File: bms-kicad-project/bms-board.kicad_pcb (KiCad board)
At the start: 4 copper layers, 134 parts, among them J1 12402012E212A, J2 DEBUG, J3 Conn_02x18_Odd_Even, J4 Conn_02x18_Odd_Even, Q1 BSS308PE_H6327, Q10 BSS308PE_H6327, Q11 BSS308PE_H6327, Q12 BSS308PE_H6327, Q13 BSS308PE_H6327, Q2 BSS308PE_H6327, Q3 BSS308PE_H6327, Q4 BSS308PE_H6327, Q5 BSS308PE_H6327, Q6 BSS308PE_H6327, Q7 BSS308PE_H6327, Q8 BSS308PE_H6327, Q9 BSS308PE_H6327, SW1 KMR223G LFG, SW2 KMR223G LFG, U1 LTC6804-2, U2 W25Q128JVSIQ TR, U3 NCP1117ST33T3G, U4 RP2040, X1 ABM8-272-T3

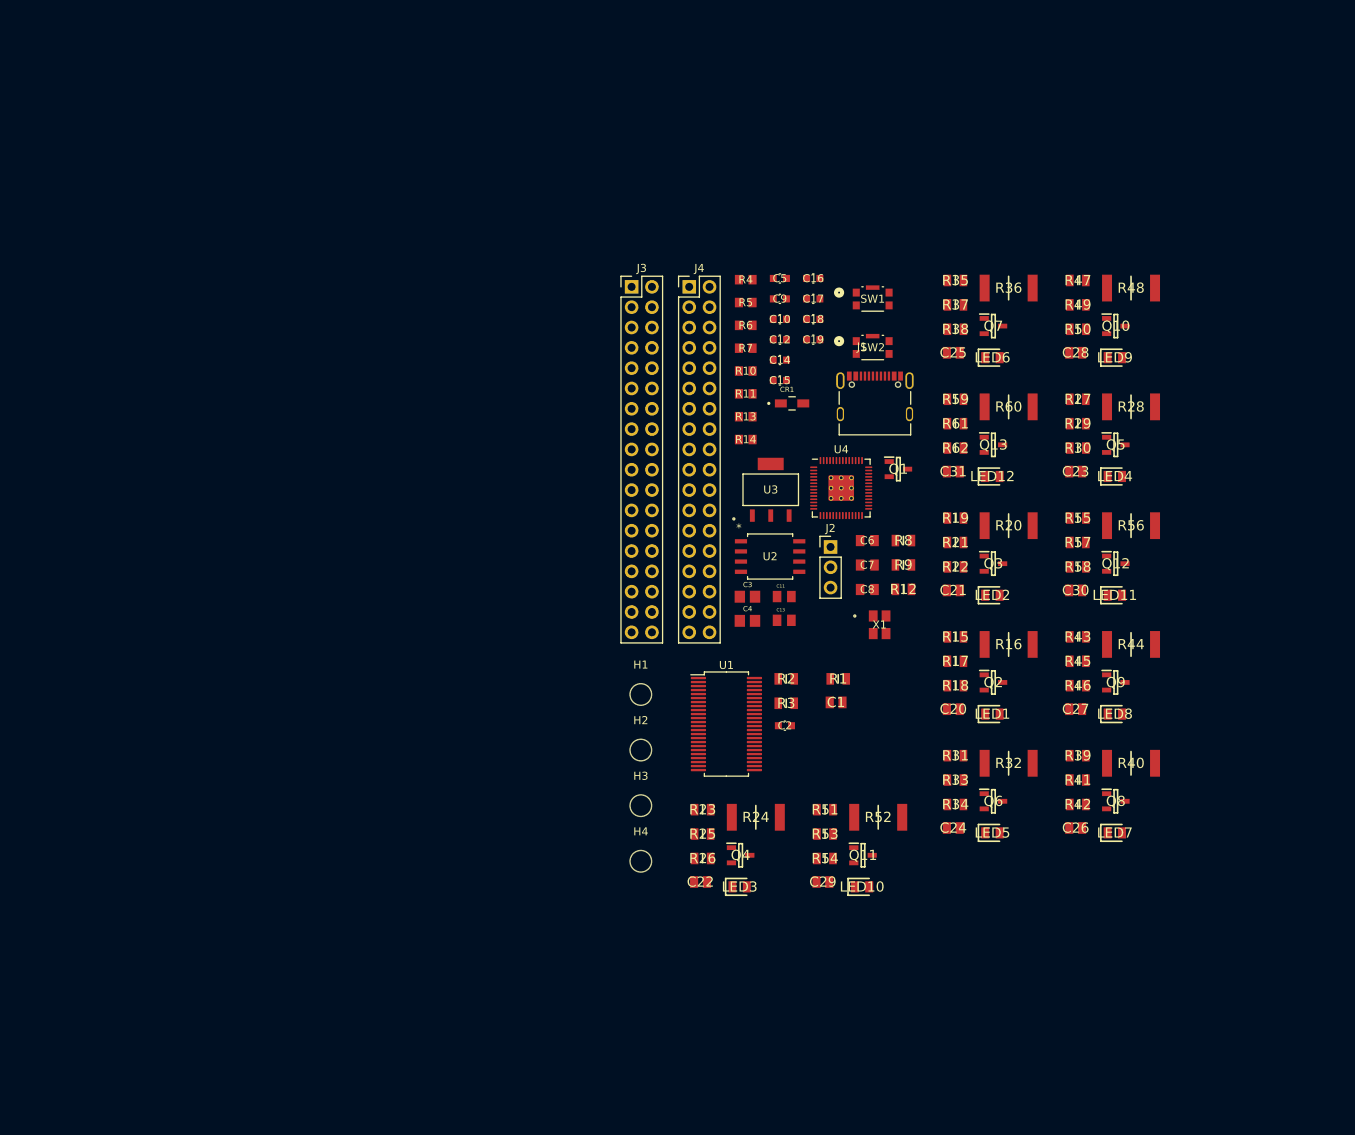
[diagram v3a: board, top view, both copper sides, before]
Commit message: feat: Added 0OHM jumper between ULTRASONIC and VDD, added LED indicator for PGOOD
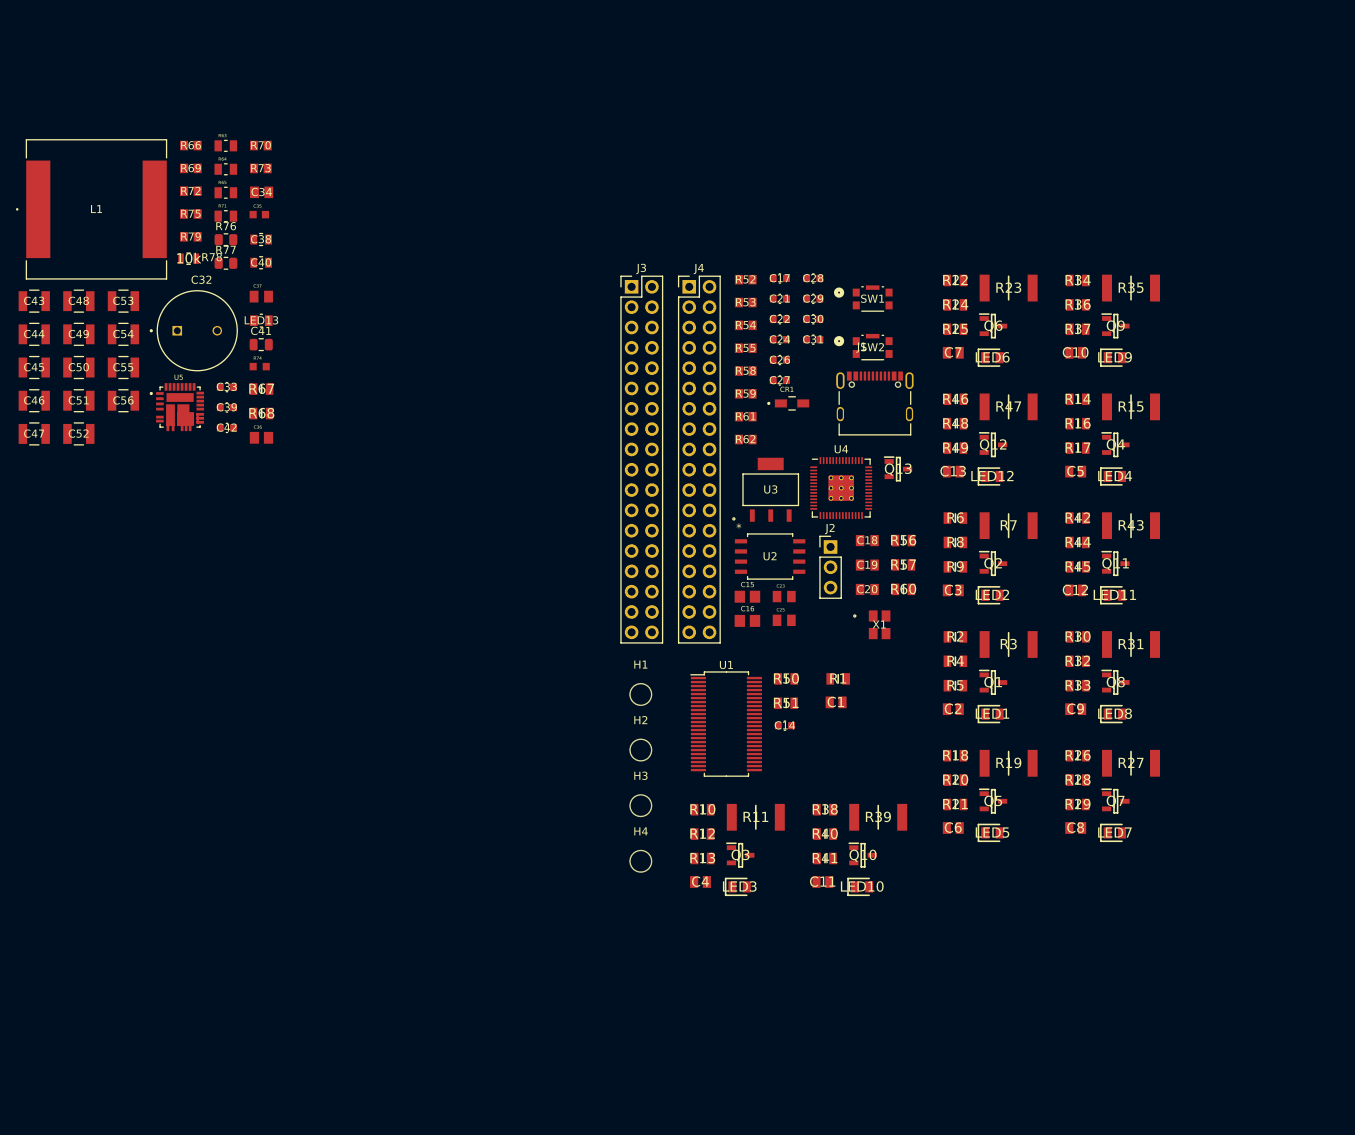
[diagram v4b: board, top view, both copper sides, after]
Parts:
- added C32: 220u, FixedWing:CAPPRD500W60D1000H2500, F.Cu at (52.3, 68.4)
- added C33: 0.1µ, FixedWing:CAP_GCJ-18_MUR, F.Cu at (56.0, 75.4)
- added C34: 560p, FixedWing:CAP_CC0805_YAG, F.Cu at (60.3, 51.1)
- added C35: 1u, FixedWing:CAPC1608X90N, F.Cu at (60.0, 53.9)
- added C36: 33n, FixedWing:CAPC2012X94N, F.Cu at (60.3, 81.8)
- added C37: 4.7u, FixedWing:CAPC2012X145N, F.Cu at (60.3, 64.1)
- added C38: 3.9n, FixedWing:G-21_MUR, F.Cu at (60.3, 57.0)
- added C39: 0.1µ, FixedWing:CAP_GCJ-18_MUR, F.Cu at (56.0, 78.0)
- added C40: 1.5n, FixedWing:G-21_MUR, F.Cu at (60.3, 59.9)
- added C41: C, Capacitor_SMD:C_0805_2012Metric, F.Cu at (60.3, 70.1)
- added C42: 0.1µ, FixedWing:CAP_GCJ-18_MUR, F.Cu at (56.0, 80.5)
- added C43: 47u, FixedWing:G-32_MUR, F.Cu at (31.9, 64.7)
- added C44: 47u, FixedWing:G-32_MUR, F.Cu at (31.9, 68.8)
- added C45: 47u, FixedWing:G-32_MUR, F.Cu at (31.9, 73.0)
- added C46: 47u, FixedWing:G-32_MUR, F.Cu at (31.9, 77.1)
- added C47: 47u, FixedWing:G-32_MUR, F.Cu at (31.9, 81.3)
- added C48: 47u, FixedWing:G-32_MUR, F.Cu at (37.5, 64.7)
- added C49: 47u, FixedWing:G-32_MUR, F.Cu at (37.5, 68.8)
- added C50: 47u, FixedWing:G-32_MUR, F.Cu at (37.5, 73.0)
- added C51: 47u, FixedWing:G-32_MUR, F.Cu at (37.5, 77.1)
- added C52: 47u, FixedWing:G-32_MUR, F.Cu at (37.5, 81.3)
- added C53: 47u, FixedWing:G-32_MUR, F.Cu at (43.0, 64.7)
- added C54: 47u, FixedWing:G-32_MUR, F.Cu at (43.0, 68.8)
- added C55: 47u, FixedWing:G-32_MUR, F.Cu at (43.0, 73.0)
- added C56: 47u, FixedWing:G-32_MUR, F.Cu at (43.0, 77.1)
- added L1: 5.6u, FixedWing:IND_IHLP-6767GZ_VIS, F.Cu at (39.7, 53.2)
- added LED13: LTST-C170KGKT, FixedWing:LED_LTST-C170KGKT_LTO, F.Cu at (60.3, 67.1)
- added R63: 562k, FixedWing:RESC2012X60N, F.Cu at (55.8, 45.3)
- added R64: 100k, FixedWing:RESC2012X60N, F.Cu at (55.8, 48.2)
- added R65: 100k, FixedWing:RESC2012X60N, F.Cu at (55.8, 51.1)
- added R66: 523k, FixedWing:RC0805N_YAG, F.Cu at (51.5, 45.2)
- added R67: 100, FixedWing:RESC2012X50N, F.Cu at (60.3, 75.7)
- added R68: 475, FixedWing:RESC2012X50N, F.Cu at (60.3, 78.7)
- added R69: 1k, FixedWing:RC0805N_YAG, F.Cu at (51.5, 48.1)
- added R70: 41.2, FixedWing:RC0805N_VIS, F.Cu at (60.2, 45.2)
- added R71: 100k, FixedWing:RESC2012X60N, F.Cu at (55.8, 54.1)
- added R72: 1k, FixedWing:RC0805N_YAG, F.Cu at (51.5, 50.9)
- added R73: 93.1k, FixedWing:RC0805N_PAN, F.Cu at (60.2, 48.1)
- added R74: 3.3, FixedWing:RESC1608X55N, F.Cu at (60.1, 72.9)
- added R75: 11.5k, FixedWing:RC0805N_YAG, F.Cu at (51.5, 53.8)
- added R76: R, Resistor_SMD:R_0805_2012Metric, F.Cu at (55.9, 57.0)
- added R77: R, Resistor_SMD:R_0805_2012Metric, F.Cu at (55.9, 60.0)
- added R78: 10k, FixedWing:KOA_Speer-RK73H2A-0-0-MFG, F.Cu at (51.2, 59.4)
- added R79: 56.2k, FixedWing:RC0805N_YAG, F.Cu at (51.5, 56.7)
- added U5: SIC461ED-T1-GE3, FixedWing:CONV_SIC461ED-T1-GE3, F.Cu at (50.1, 77.9)
- R13: renamed from R26; value 3k3 -> 3.3k
- R17: renamed from R30; value 3k3 -> 3.3k
- R21: renamed from R34; value 3k3 -> 3.3k
- R25: renamed from R38; value 3k3 -> 3.3k
- R29: renamed from R42; value 3k3 -> 3.3k
- R33: renamed from R46; value 3k3 -> 3.3k
- R37: renamed from R50; value 3k3 -> 3.3k
- R41: renamed from R54; value 3k3 -> 3.3k
- R45: renamed from R58; value 3k3 -> 3.3k
- R49: renamed from R62; value 3k3 -> 3.3k
- R5: renamed from R18; value 3k3 -> 3.3k
- R50: renamed from R2; value 3k3 -> 3.3k
- R56: renamed from R8; value 3k3 -> 3.3k
- R57: renamed from R9; value 3k3 -> 3.3k
- R60: renamed from R12; value 3k3 -> 3.3k
- R9: renamed from R22; value 3k3 -> 3.3k
- renumbered C28 to C10, C29 to C11, C30 to C12, C31 to C13, C2 to C14, C3 to C15, C4 to C16, C5 to C17, C6 to C18, C7 to C19, C20 to C2, C8 to C20, C9 to C21, C10 to C22, C11 to C23, C12 to C24, C13 to C25, C14 to C26, C15 to C27, C16 to C28, C17 to C29, C21 to C3, C18 to C30, C19 to C31, C22 to C4, C23 to C5, C24 to C6, C25 to C7, C26 to C8, C27 to C9, Q2 to Q1, Q11 to Q10, Q12 to Q11, Q13 to Q12, Q1 to Q13, Q3 to Q2, Q4 to Q3, Q5 to Q4, Q6 to Q5, Q7 to Q6, Q8 to Q7, Q9 to Q8, Q10 to Q9, R23 to R10, R24 to R11, R25 to R12, R27 to R14, R28 to R15, R29 to R16, R31 to R18, R32 to R19, R15 to R2, R33 to R20, R35 to R22, R36 to R23, R37 to R24, R39 to R26, R40 to R27, R41 to R28, R16 to R3, R43 to R30, R44 to R31, R45 to R32, R47 to R34, R48 to R35, R49 to R36, R51 to R38, R52 to R39, R17 to R4, R53 to R40, R55 to R42, R56 to R43, R57 to R44, R59 to R46, R60 to R47, R61 to R48, R3 to R51, R4 to R52, R5 to R53, R6 to R54, R7 to R55, R10 to R58, R11 to R59, R19 to R6, R13 to R61, R14 to R62, R20 to R7, R21 to R8
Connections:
- C1 pad 2: GND -> +5V
- C14 pad 2: GND -> +5V
- C15 pad 1: GND -> +5V
- C16 pad 1: GND -> +5V
- C17 pad 1: GND -> +5V
- C18 pad 1: GND -> +5V
- C19 pad 2: GND -> +5V
- C20 pad 1: GND -> +5V
- C21 pad 1: GND -> +5V
- C22 pad 1: GND -> +5V
- C23 pad 1: GND -> +5V
- C24 pad 1: GND -> +5V
- C25 pad 1: GND -> +5V
- C26 pad 1: GND -> +5V
- C27 pad 1: GND -> +5V
- C28 pad 1: GND -> +5V
- C29 pad 1: GND -> +5V
- C30 pad 1: GND -> +5V
- C31 pad 1: GND -> +5V
- J1 pad A1_B12: GND -> +5V
- J1 pad B1_A12: GND -> +5V
- J1 pad SH1: GND -> +5V
- J1 pad SH2: GND -> +5V
- J1 pad SH3: GND -> +5V
- J1 pad SH4: GND -> +5V
- J2 pad 2: GND -> +5V
- J3 pad 1: GND -> +5V
- J3 pad 11: GND -> +5V
- J3 pad 13: GND -> +5V
- J3 pad 15: GND -> +5V
- J3 pad 17: GND -> +5V
- J3 pad 19: GND -> +5V
- J3 pad 21: GND -> +5V
- J3 pad 23: GND -> +5V
- J3 pad 25: GND -> +5V
- J3 pad 27: GND -> +5V
- J3 pad 29: GND -> +5V
- J3 pad 3: GND -> +5V
- J3 pad 31: GND -> +5V
- J3 pad 33: GND -> +5V
- J3 pad 35: GND -> +5V
- J3 pad 36: GND -> +5V
- J3 pad 5: GND -> +5V
- J3 pad 7: GND -> +5V
- J3 pad 9: GND -> +5V
- J4 pad 10: GND -> +5V
- J4 pad 12: GND -> +5V
- J4 pad 14: GND -> +5V
- J4 pad 16: GND -> +5V
- J4 pad 18: GND -> +5V
- J4 pad 2: GND -> +5V
- J4 pad 20: GND -> +5V
- J4 pad 22: GND -> +5V
- J4 pad 24: GND -> +5V
- J4 pad 26: GND -> +5V
- J4 pad 28: GND -> +5V
- J4 pad 30: GND -> +5V
- J4 pad 32: GND -> +5V
- J4 pad 34: GND -> +5V
- J4 pad 35: GND -> +5V
- J4 pad 36: GND -> +5V
- J4 pad 4: GND -> +5V
- J4 pad 6: GND -> +5V
- J4 pad 8: GND -> +5V
- R2 pad 1: GND -> +5V
- R3 pad 1: GND -> +5V
- R4 pad 1: GND -> +5V
- R52 pad 2: GND -> +5V
- R53 pad 2: GND -> +5V
- SW1 pad 3: GND -> +5V
- SW1 pad 4: GND -> +5V
- SW1 pad 5: GND -> +5V
- SW2 pad 3: GND -> +5V
- SW2 pad 4: GND -> +5V
- SW2 pad 5: GND -> +5V
- U1 pad 30: GND -> +5V
- U1 pad 31: GND -> +5V
- U1 pad 40: GND -> +5V
- U3 pad 1: GND -> +5V
- U4 pad 19: GND -> +5V
- U4 pad 57: GND -> +5V
- X1 pad 2: GND -> +5V
- X1 pad 4: GND -> +5V

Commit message: feat: added buncha shit, refer to tasks 4 and 8
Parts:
- added H5: MountingHole_Pad, MountingHole:MountingHole_3.2mm_M3_Pad_Via, F.Cu at (148.0, 88.7)
- added H6: MountingHole_Pad, MountingHole:MountingHole_3.2mm_M3_Pad_Via, F.Cu at (148.0, 96.7)
- added H7: MountingHole_Pad, MountingHole:MountingHole_3.2mm_M3_Pad_Via, F.Cu at (156.0, 88.7)
- added H8: MountingHole_Pad, MountingHole:MountingHole_3.2mm_M3_Pad_Via, F.Cu at (156.0, 96.7)
- added L10: 600Ω, FixedWing:IND_BLM31PG391SN1L_MUR, F.Cu at (159.1, 75.5)
- added L11: 600Ω, FixedWing:IND_BLM31PG391SN1L_MUR, F.Cu at (164.9, 61.7)
- added L12: 600Ω, FixedWing:IND_BLM31PG391SN1L_MUR, F.Cu at (164.9, 65.1)
- added L13: 600Ω, FixedWing:IND_BLM31PG391SN1L_MUR, F.Cu at (164.9, 68.6)
- added L14: 600Ω, FixedWing:IND_BLM31PG391SN1L_MUR, F.Cu at (164.9, 72.1)
- added L15: 600Ω, FixedWing:IND_BLM31PG391SN1L_MUR, F.Cu at (175.3, 86.5)
- added L16: 5.6u, FixedWing:IND_IHLP-6767GZ_VIS, F.Cu at (99.3, 119.2)
- added L2: 600Ω, FixedWing:IND_BLM31PG391SN1L_MUR, F.Cu at (153.3, 65.1)
- added L3: 600Ω, FixedWing:IND_BLM31PG391SN1L_MUR, F.Cu at (153.3, 68.6)
- added L4: 600Ω, FixedWing:IND_BLM31PG391SN1L_MUR, F.Cu at (153.3, 72.1)
- added L5: 600Ω, FixedWing:IND_BLM31PG391SN1L_MUR, F.Cu at (153.3, 75.5)
- added L6: 600Ω, FixedWing:IND_BLM31PG391SN1L_MUR, F.Cu at (159.1, 61.7)
- added L7: 600Ω, FixedWing:IND_BLM31PG391SN1L_MUR, F.Cu at (159.1, 65.1)
- added L8: 600Ω, FixedWing:IND_BLM31PG391SN1L_MUR, F.Cu at (159.1, 68.6)
- added L9: 600Ω, FixedWing:IND_BLM31PG391SN1L_MUR, F.Cu at (159.1, 72.1)
- added R80: 1k, FixedWing:RC0805N_YAG, F.Cu at (114.8, 96.0)
- added R81: 5.6k, FixedWing:RESC2012X60N, F.Cu at (116.6, 82.6)
- added R82: 27, FixedWing:RC0805N_YAG, F.Cu at (114.8, 98.9)
- added R83: 27, FixedWing:RC0805N_YAG, F.Cu at (114.8, 101.7)
- added R84: 562k, FixedWing:RESC2012X60N, F.Cu at (115.5, 111.2)
- added R85: 100k, FixedWing:RESC2012X60N, F.Cu at (115.5, 114.1)
- added R86: 100k, FixedWing:RESC2012X60N, F.Cu at (115.5, 117.1)
- added R87: 1k, FixedWing:RC0805N_YAG, F.Cu at (111.1, 111.2)
- added R88: 5.6k, FixedWing:RESC2012X60N, F.Cu at (115.5, 120.0)
- added R89: 1k, FixedWing:RC0805N_YAG, F.Cu at (111.1, 114.0)
- added R90: 41.2, FixedWing:RC0805N_VIS, F.Cu at (119.8, 122.9)
- added R91: 93.1k, FixedWing:RC0805N_PAN, F.Cu at (119.8, 125.8)
- added R92: 523k, FixedWing:RC0805N_YAG, F.Cu at (111.1, 116.9)
- added R93: 0, FixedWing:RC1206N_YAG, F.Cu at (120.4, 111.4)
- added R94: 3.3, FixedWing:RESC1608X55N, F.Cu at (119.7, 135.8)
- added R95: 10k, FixedWing:KOA_Speer-RK73H2A-0-0-MFG, F.Cu at (110.8, 125.3)
- added R96: 11.5k, FixedWing:RC0805N_YAG, F.Cu at (111.1, 119.7)
- added R97: R, Resistor_SMD:R_0805_2012Metric, F.Cu at (119.9, 141.6)
- added R98: R, Resistor_SMD:R_0805_2012Metric, F.Cu at (119.9, 144.5)
- added R99: 56.2k, FixedWing:RC0805N_YAG, F.Cu at (111.1, 122.6)
- C34: value 560p -> 33n; footprint FixedWing:CAP_CC0805_YAG -> FixedWing:CAPC2012X94N
- C36: value 33n -> 560p; footprint FixedWing:CAPC2012X94N -> FixedWing:CAP_CC0805_YAG
- H1, H2, H3, H4: value MountingHole -> MountingHole_Pad; footprint MountingHole:MountingHole_2.7mm_M2.5 -> MountingHole:MountingHole_3.2mm_M3_Pad_Via
- L1: value 5.6u -> 600Ω; footprint FixedWing:IND_IHLP-6767GZ_VIS -> FixedWing:IND_BLM31PG391SN1L_MUR
- LED13: value LTST-C170KGKT -> LTST-C170KRKT; footprint FixedWing:LED_LTST-C170KGKT_LTO -> FixedWing:LEDC2012X120N
- R10, R14, R18, R2, R22, R26, R6: value 475 -> 0; footprint FixedWing:RESC2012X50N -> FixedWing:RC1206N_YAG
- R11, R15, R19, R23, R3, R7: value 33 -> 0; footprint FixedWing:RESC6332X70N -> FixedWing:RC1206N_YAG
- R12, R16, R20, R24, R4, R8: value 100 -> 0; footprint FixedWing:RESC2012X50N -> FixedWing:RC1206N_YAG
- R13, R17, R21, R25, R5, R9: value 3.3k -> 0; footprint FixedWing:RESC2012X50N -> FixedWing:RC1206N_YAG
- R27, R31, R35, R39, R43, R47: value 33 -> 475; footprint FixedWing:RESC6332X70N -> FixedWing:RESC2012X50N
- R28, R32, R36, R40, R44, R48: value 100 -> 33; footprint FixedWing:RESC2012X50N -> FixedWing:RC2512N_VIS
- R29, R33, R37, R41, R45, R49, R57: value 3.3k -> 100
- R30, R34, R38, R42, R46: value 475 -> 3.3k
- R51, R67: value 100 -> 475
- R52, R72: value 1k -> 33; footprint FixedWing:RC0805N_YAG -> FixedWing:RC2512N_VIS
- R53, R69: value 1k -> 100; footprint FixedWing:RC0805N_YAG -> FixedWing:RESC2012X50N
- R54, R58: value 1k -> 3.3k; footprint FixedWing:RC0805N_YAG -> FixedWing:RESC2012X50N
- R55, R59: value 1k -> 475; footprint FixedWing:RC0805N_YAG -> FixedWing:RESC2012X50N
- R56, R60: value 3.3k -> 33; footprint FixedWing:RESC2012X50N -> FixedWing:RC2512N_VIS
- R61: value 27 -> 100; footprint FixedWing:RC0805N_YAG -> FixedWing:RESC2012X50N
- R62: value 27 -> 3.3k; footprint FixedWing:RC0805N_YAG -> FixedWing:RESC2012X50N
- R63: value 562k -> 475; footprint FixedWing:RESC2012X60N -> FixedWing:RESC2012X50N
- R64: value 100k -> 33; footprint FixedWing:RESC2012X60N -> FixedWing:RC2512N_VIS
- R65: value 100k -> 100; footprint FixedWing:RESC2012X60N -> FixedWing:RESC2012X50N
- R66: value 523k -> 3.3k; footprint FixedWing:RC0805N_YAG -> FixedWing:RESC2012X50N
- R68: value 475 -> 33; footprint FixedWing:RESC2012X50N -> FixedWing:RC2512N_VIS
- R70: value 41.2 -> 3.3k; footprint FixedWing:RC0805N_VIS -> FixedWing:RESC2012X50N
- R71: value 100k -> 475; footprint FixedWing:RESC2012X60N -> FixedWing:RESC2012X50N
- R73: value 93.1k -> 100; footprint FixedWing:RC0805N_PAN -> FixedWing:RESC2012X50N
- R74: value 3.3 -> 3.3k; footprint FixedWing:RESC1608X55N -> FixedWing:RESC2012X50N
- R75: value 11.5k -> 5.6k; footprint FixedWing:RC0805N_YAG -> FixedWing:RESC2012X60N
- R76: value R -> 100; footprint Resistor_SMD:R_0805_2012Metric -> FixedWing:RESC2012X50N
- R77: value R -> 5.6k; footprint Resistor_SMD:R_0805_2012Metric -> FixedWing:RESC2012X60N
- R78: value 10k -> 5.6k; footprint FixedWing:KOA_Speer-RK73H2A-0-0-MFG -> FixedWing:RESC2012X60N
- R79: value 56.2k -> 1k
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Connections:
- C1 pad 1: /Battery Stack Monitor/C0 -> /Cell Filtering and Balancing/Filter and Balance Cell 1/C(n-1)
- C1 pad 2: +5V -> GND
- C10 pad 1: /Battery Stack Monitor/C9 -> /Cell Filtering and Balancing/Filter and Balance Cell 10/C(n-1)
- C10 pad 2: /Battery Stack Monitor/C8 -> /Cell Filtering and Balancing/Filter and Balance Cell 8/C(n)
- C11 pad 1: /Cell Filtering and Balancing/C10 -> /Cell Filtering and Balancing/Filter and Balance Cell 10/C(n)
- C11 pad 2: /Battery Stack Monitor/C9 -> /Cell Filtering and Balancing/Filter and Balance Cell 10/C(n-1)
- C12 pad 1: /Cell Filtering and Balancing/C11 -> /Cell Filtering and Balancing/Filter and Balance Cell 11/C(n)
- C12 pad 2: /Cell Filtering and Balancing/C10 -> /Cell Filtering and Balancing/Filter and Balance Cell 10/C(n)
- C13 pad 1: /Battery Stack Monitor/C12 -> /Cell Filtering and Balancing/Filter and Balance Cell 12/C(n)
- C13 pad 2: /Cell Filtering and Balancing/C11 -> /Cell Filtering and Balancing/Filter and Balance Cell 11/C(n)
- C14 pad 2: +5V -> GND
- C15 pad 1: +5V -> GND
- C16 pad 1: +5V -> GND
- C17 pad 1: +5V -> GND
- C18 pad 1: +5V -> GND
- C19 pad 2: +5V -> GND
- C2 pad 1: /Battery Stack Monitor/C1 -> /Cell Filtering and Balancing/Filter and Balance Cell 1/C(n)
- C2 pad 2: /Battery Stack Monitor/C0 -> /Cell Filtering and Balancing/Filter and Balance Cell 1/C(n-1)
- C20 pad 1: +5V -> GND
- C21 pad 1: +5V -> GND
- C22 pad 1: +5V -> GND
- C23 pad 1: +5V -> GND
- C24 pad 1: +5V -> GND
- C25 pad 1: +5V -> GND
- C26 pad 1: +5V -> GND
- C27 pad 1: +5V -> GND
- C28 pad 1: +5V -> GND
- C29 pad 1: +5V -> GND
- C3 pad 1: /Battery Stack Monitor/C2 -> /Cell Filtering and Balancing/Filter and Balance Cell 2/C(n)
- C3 pad 2: /Battery Stack Monitor/C1 -> /Cell Filtering and Balancing/Filter and Balance Cell 1/C(n)
- C30 pad 1: +5V -> GND
- C31 pad 1: +5V -> GND
- C33 pad 2: +5V -> GND
- C34 pad 1: +5V -> GND
- C34 pad 2: Net-(C34-Pad2) -> Net-(U5-SS)
- C35 pad 1: Net-(U5-ULTRASONIC) -> Net-(U5-VDD)
- C35 pad 2: +5V -> GND
- C36 pad 1: +5V -> GND
- C36 pad 2: Net-(U5-SS) -> Net-(C36-Pad2)
- C37 pad 1: +5V -> GND
- C4 pad 1: /Battery Stack Monitor/C3 -> /Cell Filtering and Balancing/Filter and Balance Cell 3/C(n)
- C4 pad 2: /Battery Stack Monitor/C2 -> /Cell Filtering and Balancing/Filter and Balance Cell 2/C(n)
- C40 pad 2: Net-(C40-Pad2) -> +5V
- C41 pad 2: +5V -> GND
- C42 pad 1: +5V -> GND
- C42 pad 2: Net-(C40-Pad2) -> +5V
- C43 pad 1: +5V -> GND
- C43 pad 2: Net-(C40-Pad2) -> +5V
- C44 pad 1: +5V -> GND
- C44 pad 2: Net-(C40-Pad2) -> +5V
- C45 pad 1: +5V -> GND
- C45 pad 2: Net-(C40-Pad2) -> +5V
- C46 pad 1: +5V -> GND
- C46 pad 2: Net-(C40-Pad2) -> +5V
- C47 pad 1: +5V -> GND
- C47 pad 2: Net-(C40-Pad2) -> +5V
- C48 pad 1: +5V -> GND
- C48 pad 2: Net-(C40-Pad2) -> +5V
- C49 pad 1: +5V -> GND
- C49 pad 2: Net-(C40-Pad2) -> +5V
- C5 pad 1: /Cell Filtering and Balancing/C4 -> /Cell Filtering and Balancing/Filter and Balance Cell 4/C(n)
- C5 pad 2: /Battery Stack Monitor/C3 -> /Cell Filtering and Balancing/Filter and Balance Cell 3/C(n)
- C50 pad 1: +5V -> GND
- C50 pad 2: Net-(C40-Pad2) -> +5V
- C51 pad 1: +5V -> GND
- C51 pad 2: Net-(C40-Pad2) -> +5V
- C52 pad 1: +5V -> GND
- C52 pad 2: Net-(C40-Pad2) -> +5V
- C53 pad 1: +5V -> GND
- C53 pad 2: Net-(C40-Pad2) -> +5V
- C54 pad 1: +5V -> GND
- C54 pad 2: Net-(C40-Pad2) -> +5V
- C55 pad 1: +5V -> GND
- C55 pad 2: Net-(C40-Pad2) -> +5V
- C56 pad 1: +5V -> GND
- C56 pad 2: Net-(C40-Pad2) -> +5V
- C6 pad 1: /Cell Filtering and Balancing/C5 -> /Cell Filtering and Balancing/Filter and Balance Cell 5/C(n)
- C6 pad 2: /Cell Filtering and Balancing/C4 -> /Cell Filtering and Balancing/Filter and Balance Cell 4/C(n)
- C7 pad 1: /Battery Stack Monitor/C6 -> /Cell Filtering and Balancing/Filter and Balance Cell 6/C(n)
- C7 pad 2: /Cell Filtering and Balancing/C5 -> /Cell Filtering and Balancing/Filter and Balance Cell 5/C(n)
- C8 pad 1: /Battery Stack Monitor/C7 -> /Cell Filtering and Balancing/Filter and Balance Cell 7/C(n)
- C8 pad 2: /Battery Stack Monitor/C6 -> /Cell Filtering and Balancing/Filter and Balance Cell 6/C(n)
- C9 pad 1: /Battery Stack Monitor/C8 -> /Cell Filtering and Balancing/Filter and Balance Cell 8/C(n)
- C9 pad 2: /Battery Stack Monitor/C7 -> /Cell Filtering and Balancing/Filter and Balance Cell 7/C(n)
- J1 pad A1_B12: +5V -> GND
- J1 pad B1_A12: +5V -> GND
- J1 pad SH1: +5V -> GND
- J1 pad SH2: +5V -> GND
- J1 pad SH3: +5V -> GND
- J1 pad SH4: +5V -> GND
- J2 pad 2: +5V -> GND
- J3 pad 1: +5V -> GND
- J3 pad 11: +5V -> GND
- J3 pad 13: +5V -> GND
- J3 pad 15: +5V -> GND
- J3 pad 17: +5V -> GND
- J3 pad 19: +5V -> GND
- J3 pad 21: +5V -> GND
- J3 pad 23: +5V -> GND
- J3 pad 25: +5V -> GND
- J3 pad 27: +5V -> GND
- J3 pad 29: +5V -> GND
- J3 pad 3: +5V -> GND
- J3 pad 31: +5V -> GND
- J3 pad 33: +5V -> GND
- J3 pad 35: +5V -> GND
- J3 pad 36: +5V -> GND
- J3 pad 5: +5V -> GND
- J3 pad 7: +5V -> GND
- J3 pad 9: +5V -> GND
- J4 pad 10: +5V -> GND
- J4 pad 12: +5V -> GND
- J4 pad 14: +5V -> GND
- J4 pad 16: +5V -> GND
- J4 pad 18: +5V -> GND
- J4 pad 2: +5V -> GND
- J4 pad 20: +5V -> GND
- J4 pad 22: +5V -> GND
- J4 pad 24: +5V -> GND
- J4 pad 26: +5V -> GND
- J4 pad 28: +5V -> GND
- J4 pad 30: +5V -> GND
- J4 pad 32: +5V -> GND
- J4 pad 34: +5V -> GND
- J4 pad 35: +5V -> GND
- J4 pad 36: +5V -> GND
- J4 pad 4: +5V -> GND
- J4 pad 6: +5V -> GND
- J4 pad 8: +5V -> GND
- L1 pad 1: Net-(U5-SW) -> /Cell Filtering and Balancing/Filter and Balance Cell 12/BATT(n)
- L1 pad 2: Net-(C40-Pad2) -> unconnected-(L1-Pad2)
- LED13 pad 1: +5V -> Net-(LED13-K)
- LED13 pad 2: Net-(LED13-A) -> GND
- R1 pad 2: /Battery Stack Monitor/C12 -> /Cell Filtering and Balancing/Filter and Balance Cell 12/C(n)
- R10 pad 1: /Cell Filtering and Balancing/Filter and Balance Cell 2/BATT(n) -> /Cell Filtering and Balancing/Filter and Balance Cell 4/C(n)
- R10 pad 2: Net-(LED3-K) -> /Battery Stack Monitor/C4
- R11 pad 1: /Cell Filtering and Balancing/Filter and Balance Cell 2/BATT(n) -> /Cell Filtering and Balancing/Filter and Balance Cell 3/C(n)
- R11 pad 2: Net-(LED3-A) -> /Battery Stack Monitor/C3
- R12 pad 1: /Cell Filtering and Balancing/Filter and Balance Cell 2/BATT(n) -> /Cell Filtering and Balancing/Filter and Balance Cell 2/C(n)
- R13 pad 1: /Battery Stack Monitor/S3 -> /Cell Filtering and Balancing/Filter and Balance Cell 1/C(n)
- R13 pad 2: Net-(Q3-G) -> /Battery Stack Monitor/C1
- R14 pad 1: /Cell Filtering and Balancing/Filter and Balance Cell 3/BATT(n) -> /Cell Filtering and Balancing/Filter and Balance Cell 1/C(n-1)
- R14 pad 2: Net-(LED4-K) -> /Battery Stack Monitor/C0
- R15 pad 1: /Cell Filtering and Balancing/Filter and Balance Cell 3/BATT(n) -> /Cell Filtering and Balancing/Filter and Balance Cell 12/S(n)
- R15 pad 2: Net-(LED4-A) -> /Battery Stack Monitor/S12
- R16 pad 1: /Cell Filtering and Balancing/Filter and Balance Cell 3/BATT(n) -> /Cell Filtering and Balancing/Filter and Balance Cell 11/S(n)
- R16 pad 2: /Battery Stack Monitor/C3 -> /Battery Stack Monitor/S11
- R17 pad 1: /Cell Filtering and Balancing/S4 -> /Cell Filtering and Balancing/Filter and Balance Cell 10/S(n)
- R17 pad 2: Net-(Q4-G) -> /Battery Stack Monitor/S10
- R18 pad 1: /Cell Filtering and Balancing/Filter and Balance Cell 4/BATT(n) -> /Cell Filtering and Balancing/Filter and Balance Cell 9/S(n)
- R18 pad 2: Net-(LED5-K) -> /Battery Stack Monitor/S9
- R19 pad 1: /Cell Filtering and Balancing/Filter and Balance Cell 4/BATT(n) -> /Cell Filtering and Balancing/Filter and Balance Cell 8/S(n)
- R19 pad 2: Net-(LED5-A) -> /Battery Stack Monitor/S8
- R2 pad 1: +5V -> /Cell Filtering and Balancing/Filter and Balance Cell 12/C(n)
- R2 pad 2: Net-(LED1-K) -> /Battery Stack Monitor/C12
- R20 pad 1: /Cell Filtering and Balancing/Filter and Balance Cell 4/BATT(n) -> /Cell Filtering and Balancing/Filter and Balance Cell 7/S(n)
- R20 pad 2: /Cell Filtering and Balancing/C4 -> /Battery Stack Monitor/S7
- R21 pad 1: /Cell Filtering and Balancing/S5 -> /Cell Filtering and Balancing/Filter and Balance Cell 6/S(n)
- R21 pad 2: Net-(Q5-G) -> /Battery Stack Monitor/S6
- R22 pad 1: /Cell Filtering and Balancing/Filter and Balance Cell 5/BATT(n) -> /Cell Filtering and Balancing/Filter and Balance Cell 5/S(n)
- R22 pad 2: Net-(LED6-K) -> /Battery Stack Monitor/S5
- R23 pad 1: /Cell Filtering and Balancing/Filter and Balance Cell 5/BATT(n) -> /Cell Filtering and Balancing/Filter and Balance Cell 4/S(n)
- R23 pad 2: Net-(LED6-A) -> /Battery Stack Monitor/S4
- R24 pad 1: /Cell Filtering and Balancing/Filter and Balance Cell 5/BATT(n) -> /Cell Filtering and Balancing/Filter and Balance Cell 3/S(n)
- R24 pad 2: /Cell Filtering and Balancing/C5 -> /Battery Stack Monitor/S3
- R25 pad 1: /Cell Filtering and Balancing/S6 -> /Cell Filtering and Balancing/Filter and Balance Cell 2/S(n)
- R25 pad 2: Net-(Q6-G) -> /Battery Stack Monitor/S2
- R26 pad 1: /Cell Filtering and Balancing/Filter and Balance Cell 6/BATT(n) -> /Cell Filtering and Balancing/Filter and Balance Cell 1/S(n)
- R26 pad 2: Net-(LED7-K) -> /Battery Stack Monitor/S1
- R27 pad 1: /Cell Filtering and Balancing/Filter and Balance Cell 6/BATT(n) -> /Cell Filtering and Balancing/Filter and Balance Cell 1/BATT(n-1)
- R27 pad 2: Net-(LED7-A) -> Net-(LED1-K)
- R28 pad 1: /Cell Filtering and Balancing/Filter and Balance Cell 6/BATT(n) -> /Cell Filtering and Balancing/Filter and Balance Cell 1/BATT(n-1)
- R28 pad 2: /Battery Stack Monitor/C6 -> Net-(LED1-A)
- R29 pad 1: /Battery Stack Monitor/S7 -> /Cell Filtering and Balancing/Filter and Balance Cell 1/BATT(n-1)
- R29 pad 2: Net-(Q7-G) -> /Cell Filtering and Balancing/Filter and Balance Cell 1/C(n-1)
- R3 pad 1: +5V -> /Cell Filtering and Balancing/Filter and Balance Cell 11/C(n)
- R3 pad 2: Net-(LED1-A) -> /Battery Stack Monitor/C11
- R30 pad 1: /Cell Filtering and Balancing/Filter and Balance Cell 7/BATT(n) -> /Cell Filtering and Balancing/Filter and Balance Cell 1/S(n)
- R30 pad 2: Net-(LED8-K) -> Net-(Q1-G)
- R31 pad 1: /Cell Filtering and Balancing/Filter and Balance Cell 7/BATT(n) -> /Cell Filtering and Balancing/Filter and Balance Cell 1/BATT(n)
- R31 pad 2: Net-(LED8-A) -> Net-(LED2-K)
- R32 pad 1: /Cell Filtering and Balancing/Filter and Balance Cell 7/BATT(n) -> /Cell Filtering and Balancing/Filter and Balance Cell 1/BATT(n)
- R32 pad 2: /Battery Stack Monitor/C7 -> Net-(LED2-A)
- R33 pad 1: /Battery Stack Monitor/S8 -> /Cell Filtering and Balancing/Filter and Balance Cell 1/BATT(n)
- R33 pad 2: Net-(Q8-G) -> /Cell Filtering and Balancing/Filter and Balance Cell 1/C(n)
- R34 pad 1: /Cell Filtering and Balancing/Filter and Balance Cell 8/BATT(n) -> /Cell Filtering and Balancing/Filter and Balance Cell 2/S(n)
- R34 pad 2: Net-(LED9-K) -> Net-(Q2-G)
- R35 pad 1: /Cell Filtering and Balancing/Filter and Balance Cell 8/BATT(n) -> /Cell Filtering and Balancing/Filter and Balance Cell 2/BATT(n)
- R35 pad 2: Net-(LED9-A) -> Net-(LED3-K)
- R36 pad 1: /Cell Filtering and Balancing/Filter and Balance Cell 8/BATT(n) -> /Cell Filtering and Balancing/Filter and Balance Cell 2/BATT(n)
- R36 pad 2: /Battery Stack Monitor/C8 -> Net-(LED3-A)
- R37 pad 1: /Battery Stack Monitor/S9 -> /Cell Filtering and Balancing/Filter and Balance Cell 2/BATT(n)
- R37 pad 2: Net-(Q9-G) -> /Cell Filtering and Balancing/Filter and Balance Cell 2/C(n)
- R38 pad 1: /Cell Filtering and Balancing/Filter and Balance Cell 10/BATT(n-1) -> /Cell Filtering and Balancing/Filter and Balance Cell 3/S(n)
- R38 pad 2: Net-(LED10-K) -> Net-(Q3-G)
- R39 pad 1: /Cell Filtering and Balancing/Filter and Balance Cell 10/BATT(n-1) -> /Cell Filtering and Balancing/Filter and Balance Cell 3/BATT(n)
- R39 pad 2: Net-(LED10-A) -> Net-(LED4-K)
- R4 pad 1: +5V -> /Cell Filtering and Balancing/Filter and Balance Cell 10/C(n)
- R4 pad 2: /Battery Stack Monitor/C0 -> /Battery Stack Monitor/C10
- R40 pad 1: /Cell Filtering and Balancing/Filter and Balance Cell 10/BATT(n-1) -> /Cell Filtering and Balancing/Filter and Balance Cell 3/BATT(n)
- R40 pad 2: /Battery Stack Monitor/C9 -> Net-(LED4-A)
- R41 pad 1: /Cell Filtering and Balancing/S10 -> /Cell Filtering and Balancing/Filter and Balance Cell 3/BATT(n)
- R41 pad 2: Net-(Q10-G) -> /Cell Filtering and Balancing/Filter and Balance Cell 3/C(n)
- R42 pad 1: /Cell Filtering and Balancing/Filter and Balance Cell 10/BATT(n) -> /Cell Filtering and Balancing/Filter and Balance Cell 4/S(n)
- R42 pad 2: Net-(LED11-K) -> Net-(Q4-G)
- R43 pad 1: /Cell Filtering and Balancing/Filter and Balance Cell 10/BATT(n) -> /Cell Filtering and Balancing/Filter and Balance Cell 4/BATT(n)
- R43 pad 2: Net-(LED11-A) -> Net-(LED5-K)
- R44 pad 1: /Cell Filtering and Balancing/Filter and Balance Cell 10/BATT(n) -> /Cell Filtering and Balancing/Filter and Balance Cell 4/BATT(n)
- R44 pad 2: /Cell Filtering and Balancing/C10 -> Net-(LED5-A)
- R45 pad 1: /Cell Filtering and Balancing/S11 -> /Cell Filtering and Balancing/Filter and Balance Cell 4/BATT(n)
- R45 pad 2: Net-(Q11-G) -> /Cell Filtering and Balancing/Filter and Balance Cell 4/C(n)
- R46 pad 1: /Cell Filtering and Balancing/Filter and Balance Cell 11/BATT(n) -> /Cell Filtering and Balancing/Filter and Balance Cell 5/S(n)
- R46 pad 2: Net-(LED12-K) -> Net-(Q5-G)
- R47 pad 1: /Cell Filtering and Balancing/Filter and Balance Cell 11/BATT(n) -> /Cell Filtering and Balancing/Filter and Balance Cell 5/BATT(n)
- R47 pad 2: Net-(LED12-A) -> Net-(LED6-K)
- R48 pad 1: /Cell Filtering and Balancing/Filter and Balance Cell 11/BATT(n) -> /Cell Filtering and Balancing/Filter and Balance Cell 5/BATT(n)
- R48 pad 2: /Cell Filtering and Balancing/C11 -> Net-(LED6-A)
- R49 pad 1: /Cell Filtering and Balancing/S12 -> /Cell Filtering and Balancing/Filter and Balance Cell 5/BATT(n)
- R49 pad 2: Net-(Q12-G) -> /Cell Filtering and Balancing/Filter and Balance Cell 5/C(n)
- R5 pad 1: /Battery Stack Monitor/S1 -> /Cell Filtering and Balancing/Filter and Balance Cell 10/C(n-1)
- R5 pad 2: Net-(Q1-G) -> /Battery Stack Monitor/C9
- R50 pad 1: /RP2040 Microcontroller/GPIO0 -> /Cell Filtering and Balancing/Filter and Balance Cell 6/S(n)
- R50 pad 2: +5V -> Net-(Q6-G)
- R51 pad 1: Net-(U1-V+) -> /Cell Filtering and Balancing/Filter and Balance Cell 6/BATT(n)
- R51 pad 2: +BATT -> Net-(LED7-K)
- R52 pad 1: Net-(R52-Pad1) -> /Cell Filtering and Balancing/Filter and Balance Cell 6/BATT(n)
- R52 pad 2: +5V -> Net-(LED7-A)
- R53 pad 1: Net-(R53-Pad1) -> /Cell Filtering and Balancing/Filter and Balance Cell 6/BATT(n)
- R53 pad 2: +5V -> /Cell Filtering and Balancing/Filter and Balance Cell 6/C(n)
- R54 pad 1: Net-(R54-Pad1) -> /Cell Filtering and Balancing/Filter and Balance Cell 7/S(n)
- R54 pad 2: Net-(R52-Pad1) -> Net-(Q7-G)
- R55 pad 1: Net-(R55-Pad1) -> /Cell Filtering and Balancing/Filter and Balance Cell 7/BATT(n)
- R55 pad 2: Net-(R53-Pad1) -> Net-(LED8-K)
- R56 pad 1: Net-(J1-CC1_B) -> /Cell Filtering and Balancing/Filter and Balance Cell 7/BATT(n)
- R56 pad 2: Net-(R54-Pad1) -> Net-(LED8-A)
- R57 pad 1: Net-(J1-CC1_A) -> /Cell Filtering and Balancing/Filter and Balance Cell 7/BATT(n)
- R57 pad 2: Net-(R55-Pad1) -> /Cell Filtering and Balancing/Filter and Balance Cell 7/C(n)
- R58 pad 1: Net-(C16-Pad2) -> /Cell Filtering and Balancing/Filter and Balance Cell 8/S(n)
- R58 pad 2: /RP2040 Microcontroller/XOUT -> Net-(Q8-G)
- R59 pad 1: /RP2040 Microcontroller/~{USB_BOOT} -> /Cell Filtering and Balancing/Filter and Balance Cell 8/BATT(n)
- R59 pad 2: /RP2040 Microcontroller/QSPI_SS -> Net-(LED9-K)
- R6 pad 1: /Cell Filtering and Balancing/Filter and Balance Cell 1/BATT(n) -> /Cell Filtering and Balancing/Filter and Balance Cell 8/C(n)
- R6 pad 2: Net-(LED2-K) -> /Battery Stack Monitor/C8
- R60 pad 1: /RP2040 Microcontroller/~{RESET} -> /Cell Filtering and Balancing/Filter and Balance Cell 8/BATT(n)
- R60 pad 2: +3V3 -> Net-(LED9-A)
- R61 pad 1: Net-(U4-USB_DP) -> /Cell Filtering and Balancing/Filter and Balance Cell 8/BATT(n)
- R61 pad 2: /RP2040 Microcontroller/USB_D+ -> /Cell Filtering and Balancing/Filter and Balance Cell 8/C(n)
- R62 pad 1: Net-(U4-USB_DM) -> /Cell Filtering and Balancing/Filter and Balance Cell 9/S(n)
- R62 pad 2: /RP2040 Microcontroller/USB_D- -> Net-(Q9-G)
- R63 pad 1: Net-(U5-EN) -> /Cell Filtering and Balancing/Filter and Balance Cell 10/BATT(n-1)
- R63 pad 2: +BATT -> Net-(LED10-K)
- R64 pad 1: Net-(R64-Pad1) -> /Cell Filtering and Balancing/Filter and Balance Cell 10/BATT(n-1)
- R64 pad 2: Net-(U5-EN) -> Net-(LED10-A)
- R65 pad 1: +5V -> /Cell Filtering and Balancing/Filter and Balance Cell 10/BATT(n-1)
- R65 pad 2: Net-(R64-Pad1) -> /Cell Filtering and Balancing/Filter and Balance Cell 10/C(n-1)
- R66 pad 1: Net-(C34-Pad2) -> /Cell Filtering and Balancing/Filter and Balance Cell 10/S(n)
- R66 pad 2: Net-(U5-COMP) -> Net-(Q10-G)
- R67 pad 1: Net-(LED13-A) -> /Cell Filtering and Balancing/Filter and Balance Cell 10/BATT(n)
- R67 pad 2: Net-(R67-Pad2) -> Net-(LED11-K)
- R68 pad 1: Net-(R67-Pad2) -> /Cell Filtering and Balancing/Filter and Balance Cell 10/BATT(n)
- R68 pad 2: Net-(U5-ULTRASONIC) -> Net-(LED11-A)
- R69 pad 1: +5V -> /Cell Filtering and Balancing/Filter and Balance Cell 10/BATT(n)
- R69 pad 2: Net-(R69-Pad2) -> /Cell Filtering and Balancing/Filter and Balance Cell 10/C(n)
- R7 pad 1: /Cell Filtering and Balancing/Filter and Balance Cell 1/BATT(n) -> /Cell Filtering and Balancing/Filter and Balance Cell 7/C(n)
- R7 pad 2: Net-(LED2-A) -> /Battery Stack Monitor/C7
- R70 pad 1: +5V -> /Cell Filtering and Balancing/Filter and Balance Cell 11/S(n)
- R70 pad 2: Net-(U5-ILIMIT) -> Net-(Q11-G)
- R71 pad 1: Net-(U5-ULTRASONIC) -> /Cell Filtering and Balancing/Filter and Balance Cell 11/BATT(n)
- R71 pad 2: Net-(U5-PGOOD) -> Net-(LED12-K)
- R72 pad 1: Net-(R69-Pad2) -> /Cell Filtering and Balancing/Filter and Balance Cell 11/BATT(n)
- R72 pad 2: Net-(U5-MODE) -> Net-(LED12-A)
- R73 pad 1: +5V -> /Cell Filtering and Balancing/Filter and Balance Cell 11/BATT(n)
- R73 pad 2: Net-(U5-FSW) -> /Cell Filtering and Balancing/Filter and Balance Cell 11/C(n)
- R74 pad 1: Net-(U5-BOOT) -> /Cell Filtering and Balancing/Filter and Balance Cell 12/S(n)
- R74 pad 2: Net-(C39-Pad1) -> Net-(Q12-G)
- R75 pad 1: Net-(U5-SW) -> /RP2040 Microcontroller/GPIO0
- R75 pad 2: Net-(C38-Pad2) -> +5V
- R76 pad 1: Net-(U5-SW) -> Net-(U1-V+)
- R76 pad 2: Net-(C41-Pad1) -> Net-(L15-Pad2)
- R77 pad 1: Net-(U5-SW) -> GND
- R77 pad 2: Net-(C41-Pad1) -> Net-(J1-CC1_B)
- R78 pad 1: +5V -> GND
- R78 pad 2: Net-(U5-VFB) -> Net-(J1-CC1_A)
- R79 pad 1: Net-(U5-VFB) -> Net-(C16-Pad2)
- R79 pad 2: Net-(C40-Pad2) -> /RP2040 Microcontroller/XOUT
- R8 pad 1: /Cell Filtering and Balancing/Filter and Balance Cell 1/BATT(n) -> /Cell Filtering and Balancing/Filter and Balance Cell 6/C(n)
- R8 pad 2: /Battery Stack Monitor/C1 -> /Battery Stack Monitor/C6
- R9 pad 1: /Battery Stack Monitor/S2 -> /Cell Filtering and Balancing/Filter and Balance Cell 5/C(n)
- R9 pad 2: Net-(Q2-G) -> /Battery Stack Monitor/C5
- SW1 pad 3: +5V -> GND
- SW1 pad 4: +5V -> GND
- SW1 pad 5: +5V -> GND
- SW2 pad 3: +5V -> GND
- SW2 pad 4: +5V -> GND
- SW2 pad 5: +5V -> GND
- U1 pad 15: unconnected-(U1-S6-Pad15) -> /Battery Stack Monitor/S6
- U1 pad 16: /Battery Stack Monitor/C6 -> /Battery Stack Monitor/C5
- U1 pad 17: unconnected-(U1-S5-Pad17) -> /Battery Stack Monitor/S5
- U1 pad 18: /Battery Stack Monitor/C6 -> /Battery Stack Monitor/C4
- U1 pad 19: unconnected-(U1-S4-Pad19) -> /Battery Stack Monitor/S4
- U1 pad 3: unconnected-(U1-S12-Pad3) -> /Battery Stack Monitor/S12
- U1 pad 30: +5V -> GND
- U1 pad 31: +5V -> GND
- U1 pad 4: /Battery Stack Monitor/C12 -> /Battery Stack Monitor/C11
- U1 pad 40: +5V -> GND
- U1 pad 5: unconnected-(U1-S11-Pad5) -> /Battery Stack Monitor/S11
- U1 pad 6: /Battery Stack Monitor/C12 -> /Battery Stack Monitor/C10
- U1 pad 7: unconnected-(U1-S10-Pad7) -> /Battery Stack Monitor/S10
- U3 pad 1: +5V -> GND
- U4 pad 19: +5V -> GND
- U4 pad 57: +5V -> GND
- U5 pad 10: +5V -> GND
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
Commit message: feat: finished 5V reg circuit lgtm!
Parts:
- C34: value 33n -> 560p; footprint FixedWing:CAPC2012X94N -> FixedWing:CAP_CC0805_YAG
- C36: value 560p -> 33n; footprint FixedWing:CAP_CC0805_YAG -> FixedWing:CAPC2012X94N
- LED13: value LTST-C170KRKT -> LTST-C170KGKT; footprint FixedWing:LEDC2012X120N -> FixedWing:LED_LTST-C170KGKT_LTO
- R87: value 1k -> 523k
- R88: value 5.6k -> 10k; footprint FixedWing:RESC2012X60N -> FixedWing:KOA_Speer-RK73H2A-0-0-MFG
- R91: value 93.1k -> 0; footprint FixedWing:RC0805N_PAN -> FixedWing:RC1206N_YAG
- R92: value 523k -> 1k
- R93: value 0 -> 93.1k; footprint FixedWing:RC1206N_YAG -> FixedWing:RESC2012X60N
- moved C34 40.4 mm to (115.9, 107.3)
- moved C35 24.0 mm to (106.9, 118.0)
- moved R91 21.9 mm to (116.4, 104.1)
- moved C37 11.0 mm to (115.9, 140.3)
- moved LED13 9.13 mm to (115.9, 122.8)
- moved R93 9.11 mm to (111.4, 112.8)
- moved R95 8.60 mm to (115.5, 118.1)
- moved C36 8.57 mm to (115.9, 110.4)
- moved C41 8.30 mm to (115.9, 125.8)
- moved C12 8.29 mm to (141.3, 135.5)
- moved C8 8.29 mm to (171.6, 135.5)
- moved R46 8.29 mm to (156.7, 132.6)
- moved C46 8.29 mm to (87.5, 135.8)
- moved C47 8.29 mm to (87.5, 140.0)
- moved C51 8.29 mm to (93.1, 135.8)
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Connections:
- C17 pad 1: GND -> +3V3
- C17 pad 2: +3V3 -> GND
- C18 pad 1: GND -> Net-(Q13-S)
- C18 pad 2: Net-(Q13-S) -> GND
- C19 pad 1: +3V3 -> GND
- C19 pad 2: GND -> +3V3
- C24 pad 1: GND -> +3V3
- C24 pad 2: +3V3 -> GND
- C26 pad 1: GND -> +3V3
- C26 pad 2: +3V3 -> GND
- C28 pad 1: GND -> +3V3
- C28 pad 2: +3V3 -> GND
- C29 pad 1: GND -> +3V3
- C29 pad 2: +3V3 -> GND
- C30 pad 1: GND -> +3V3
- C30 pad 2: +3V3 -> GND
- C31 pad 1: GND -> +3V3
- C31 pad 2: +3V3 -> GND
- C33 pad 1: +BATT -> GND
- C33 pad 2: GND -> +BATT
- C34 pad 2: Net-(U5-SS) -> Net-(C34-Pad2)
- C36 pad 2: Net-(C36-Pad2) -> Net-(U5-SS)
- LED13 pad 1: Net-(LED13-K) -> GND
- LED13 pad 2: GND -> Net-(LED13-A)
- R1 pad 2: /Cell Filtering and Balancing/Filter and Balance Cell 12/C(n) -> unconnected-(R1-Pad2)
- R87 pad 1: GND -> Net-(C34-Pad2)
- R87 pad 2: Net-(R87-Pad2) -> Net-(U5-COMP)
- R88 pad 2: GND -> Net-(LED13-A)
- R89 pad 1: Net-(R87-Pad2) -> GND
- R89 pad 2: Net-(U5-MODE) -> Net-(R89-Pad2)
- R91 pad 1: GND -> Net-(U5-VDD)
- R91 pad 2: Net-(U5-FSW) -> Net-(U5-ULTRASONIC)
- R92 pad 1: Net-(C36-Pad2) -> Net-(R89-Pad2)
- R92 pad 2: Net-(U5-COMP) -> Net-(U5-MODE)
- R93 pad 1: Net-(U5-VDD) -> GND
- R93 pad 2: Net-(U5-ULTRASONIC) -> Net-(U5-FSW)
- U5 pad 2: Net-(LED13-K) -> Net-(LED13-A)
